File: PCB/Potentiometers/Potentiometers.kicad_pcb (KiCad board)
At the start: 2 copper layers, 80 x 25 mm, 8 parts, among them J1 Conn_01x05

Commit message: PCB Manufacturing Files and Full CAD
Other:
- board text added: "Potentiometer Panel: PDB12-H4201-103BF Tolga Cavusoglu September 2025"
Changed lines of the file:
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@@
 		(layer "Edge.Cuts")
+	)
+	(gr_text "Potentiometer Panel: \nPDB12-H4201-103BF\nTolga Cavusoglu\nSeptember 2025"
+		(at 118.25 106.5 0)
+		(layer "B.SilkS")
+		(effects
+			(font
+				(size 1 1)
+				(thickness 0.1)
+			)
+			(justify left bottom mirror)
+		)
 	)
 	(segment

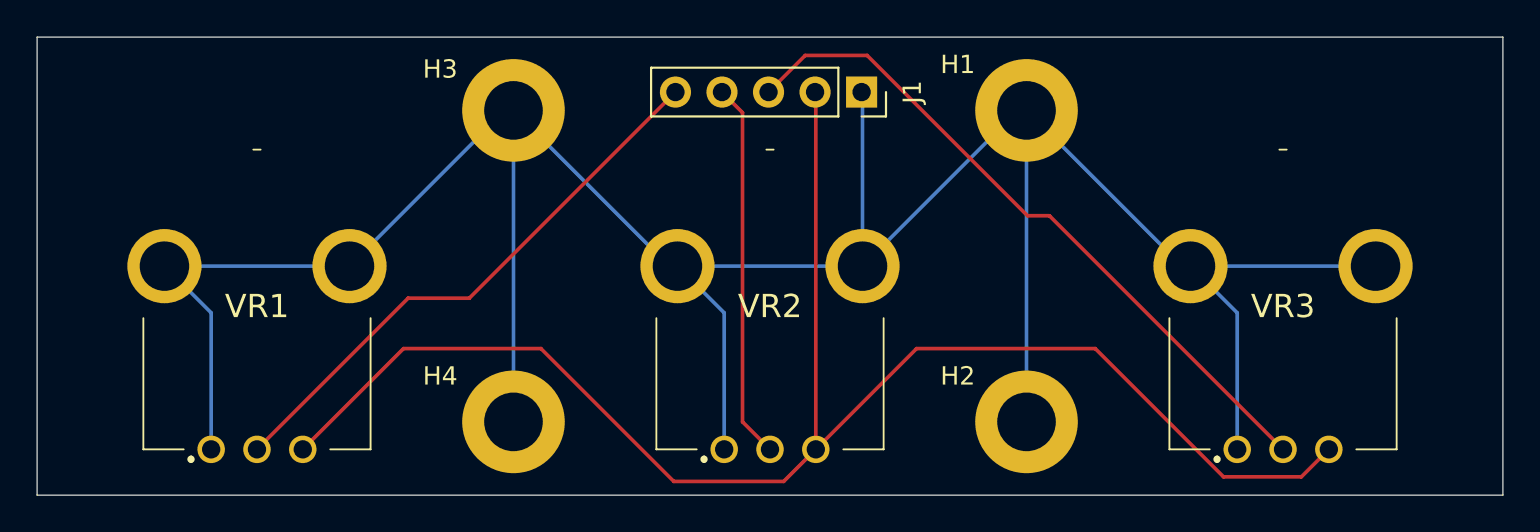
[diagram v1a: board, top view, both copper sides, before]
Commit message: Update potentiometer panel
Increase the pitch between the pins of the potentiometers to account for disagreement between footprint found online and actual component
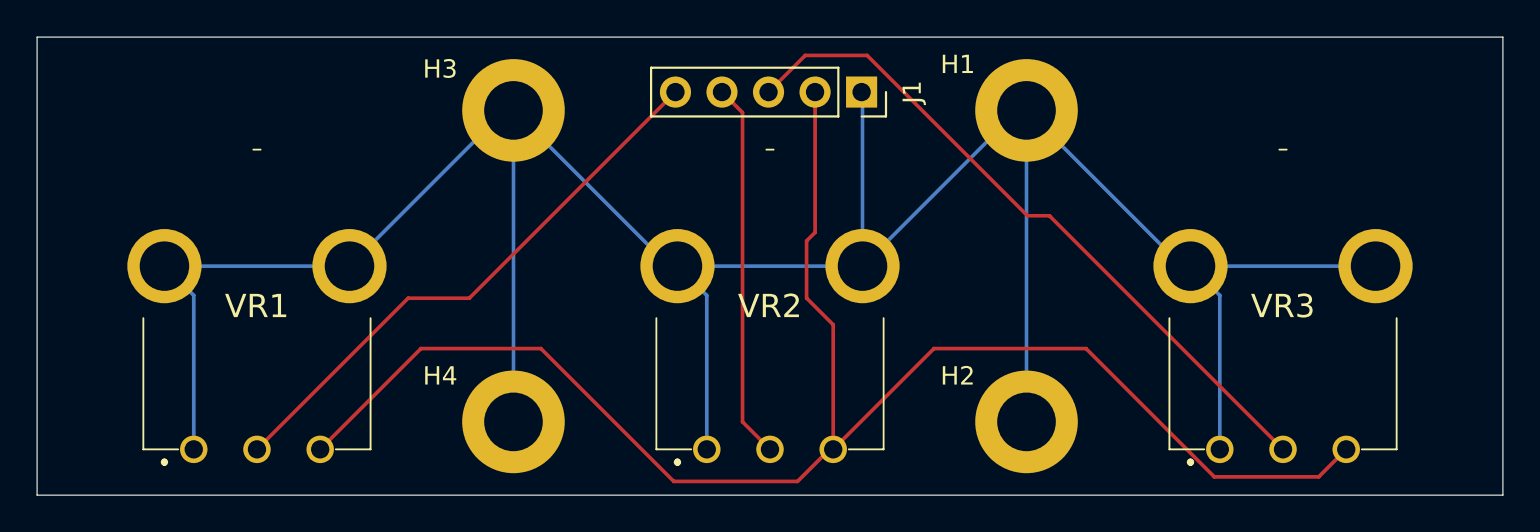
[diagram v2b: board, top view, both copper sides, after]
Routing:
- net GND: track 156.9 -> 155.7 mm
- net +3.3V: track 87.7 -> 88.7 mm
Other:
- board text added: "Potentiometer Panel v1.1: PDB12-H4201-103BF Tolga Cavusoglu September 2025"
- board text removed: "Potentiometer Panel: PDB12-H4201-103BF Tolga Cavusoglu September 2025"
